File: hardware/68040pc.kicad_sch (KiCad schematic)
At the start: 1 part, among them U1 68LC040

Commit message: lock position of expansion slots
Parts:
- added J10, J11, J12, J13, J14, J15, J8, J9: EXP, 68040:EXP, symbol 68040:EXP
- added J5: DB25_Receptacle_MountingHoles, Connector_Dsub:DSUB-25_Male_Horizontal_P2.77x2.84mm_EdgePinOffset4.94mm_Housed_MountingHolesOffset7.48mm, symbol Connector:DB25_Receptacle_MountingHoles
- added J6, J7: DE9_Plug_MountingHoles, Connector_Dsub:DSUB-9_Male_Horizontal_P2.77x2.84mm_EdgePinOffset4.94mm_Housed_MountingHolesOffset7.48mm, symbol Connector:DE9_Plug_MountingHoles
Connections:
- net GND_{O}: now reaches U1.B10 (GND)
- net GND_{O}: now also U1.B13 (GND), U1.B15 (GND), U1.B17 (GND), U1.B2 (GND), U1.B4 (GND), U1.B6 (GND), U1.B8 (GND), U1.D17 (GND), U1.D2 (GND), U1.F17 (GND), U1.F2 (GND), U1.H17 (GND), U1.H2 (GND), U1.L17 (GND), U1.L2 (GND), U1.N17 (GND), U1.N2 (GND), U1.Q17 (GND), U1.Q2 (GND), U1.S15 (GND), U1.S17 (GND), U1.S2 (GND)
- net V_{CC}_{O}: now reaches U1.B14 (V_{CC})
- net V_{CC}_{O}: now also U1.B5 (V_{CC}), U1.B9 (V_{CC}), U1.C17 (V_{CC}), U1.C2 (V_{CC}), U1.G17 (V_{CC}), U1.G2 (V_{CC}), U1.M17 (V_{CC}), U1.M2 (V_{CC}), U1.R17 (V_{CC}), U1.R2 (V_{CC}), U1.S16 (V_{CC})
- net V_{CC}_{L}: now reaches U1.C10 (V_{CC})
- net V_{CC}_{L}: now also U1.C12 (V_{CC}), U1.C14 (V_{CC}), U1.C5 (V_{CC}), U1.C8 (V_{CC}), U1.H16 (V_{CC}), U1.H3 (V_{CC}), U1.J16 (V_{CC}), U1.J3 (V_{CC}), U1.L16 (V_{CC}), U1.M3 (V_{CC}), U1.R12 (V_{CC}), U1.R5 (V_{CC})
- net GND_{L}: now reaches U1.C11 (GND)
- net GND_{L}: now also U1.C13 (GND), U1.C6 (GND), U1.C7 (GND), U1.C9 (GND), U1.K16 (GND), U1.K3 (GND), U1.L3 (GND), U1.M16 (GND), U1.R11 (GND), U1.R13 (GND), U1.R4 (GND), U1.S10 (GND), U1.T4 (GND)
- net TM2: now reaches U1.K17 (TM2)
- net TM1: now reaches U1.M18 (TM1)
- net R/~{W}: now reaches U1.N16 (R/~{W})
- net TM0: now reaches U1.N18 (TM0)
- net SIZ1: now reaches U1.P16 (SIZ1)
- net SIZ0: now reaches U1.P17 (SIZ0)
- net TLN1: now reaches U1.P18 (TLN1)
- net TT1: now reaches U1.P2 (TT1)
- net TT0: now reaches U1.P3 (TT0)
- net UPA1: now reaches U1.Q1 (UPA1)
- net ~{MI}: now reaches U1.Q16 (~{MI})
- net TLN0: now reaches U1.Q18 (TLN0)
- net UPA0: now reaches U1.Q3 (UPA0)
- net ~{CIOUT}: now reaches U1.R1 (~{CIOUT})
- net GND_{P}: now reaches U1.R10 (GND)
- net GND_{P}: now also U1.R6 (GND), U1.S9 (GND)
- net PST2: now reaches U1.R14 (PST2)
- net ~{TIP}: now reaches U1.R15 (~{TIP})
- net ~{TS}: now reaches U1.R16 (~{TS})
- net ~{LOCKE}: now reaches U1.R18 (~{LOCKE})
- net ~{RSTO}: now reaches U1.R3 (~{RSTO})
- net BCLK: now reaches U1.R7 (BCLK)
- net V_{CC}_{P}: now reaches U1.R8 (V_{CC})
- net V_{CC}_{P}: now also U1.S8 (V_{CC})
- net PCLK: now reaches U1.R9 (PCLK)
- net ~{IPEND}: now reaches U1.S1 (~{IPEND})
- net ~{TBI}: now reaches U1.S11 (~{TBI})
- net SC1: now reaches U1.S12 (SC1)
- net ~{TEA}: now reaches U1.S13 (~{TEA})
- net PST1: now reaches U1.S14 (PST1)
- net ~{LOCK}: now reaches U1.S18 (~{LOCK})
- net TDI: now reaches U1.S3 (TDI)
- net TCK: now reaches U1.S4 (TCK)
- net TMS: now reaches U1.S5 (TMS)
- net ~{MDIS}: now reaches U1.S6 (~{MDIS})
- net ~{RSTI}: now reaches U1.S7 (~{RSTI})
- net ~{TCI}: now reaches U1.T10 (~{TCI})
- net ~{AVEC}: now reaches U1.T11 (~{AVEC})
- net SC0: now reaches U1.T12 (SC0)
- net ~{BG}: now reaches U1.T13 (~{BG})
- net ~{TA}: now reaches U1.T14 (~{TA})
- net PST0: now reaches U1.T15 (PST0)
- net PST3: now reaches U1.T16 (PST3)
- net ~{BB}: now reaches U1.T17 (~{BB})
- net ~{BR}: now reaches U1.T18 (~{BR})
- net TDO: now reaches U1.T2 (TDO)
- net ~{TSRT}: now reaches U1.T3 (~{TRST})
- net ~{CDIS}: now reaches U1.T5 (~{CDIS})
- net ~{IPL2}: now reaches U1.T6 (~{IPL2})
- net ~{IPL1}: now reaches U1.T7 (~{IPL1})
- net ~{IPL0}: now reaches U1.T8 (~{IPL0})
- net JS0: now reaches U1.T9 (JS0)
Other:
- moved on the sheet: U1

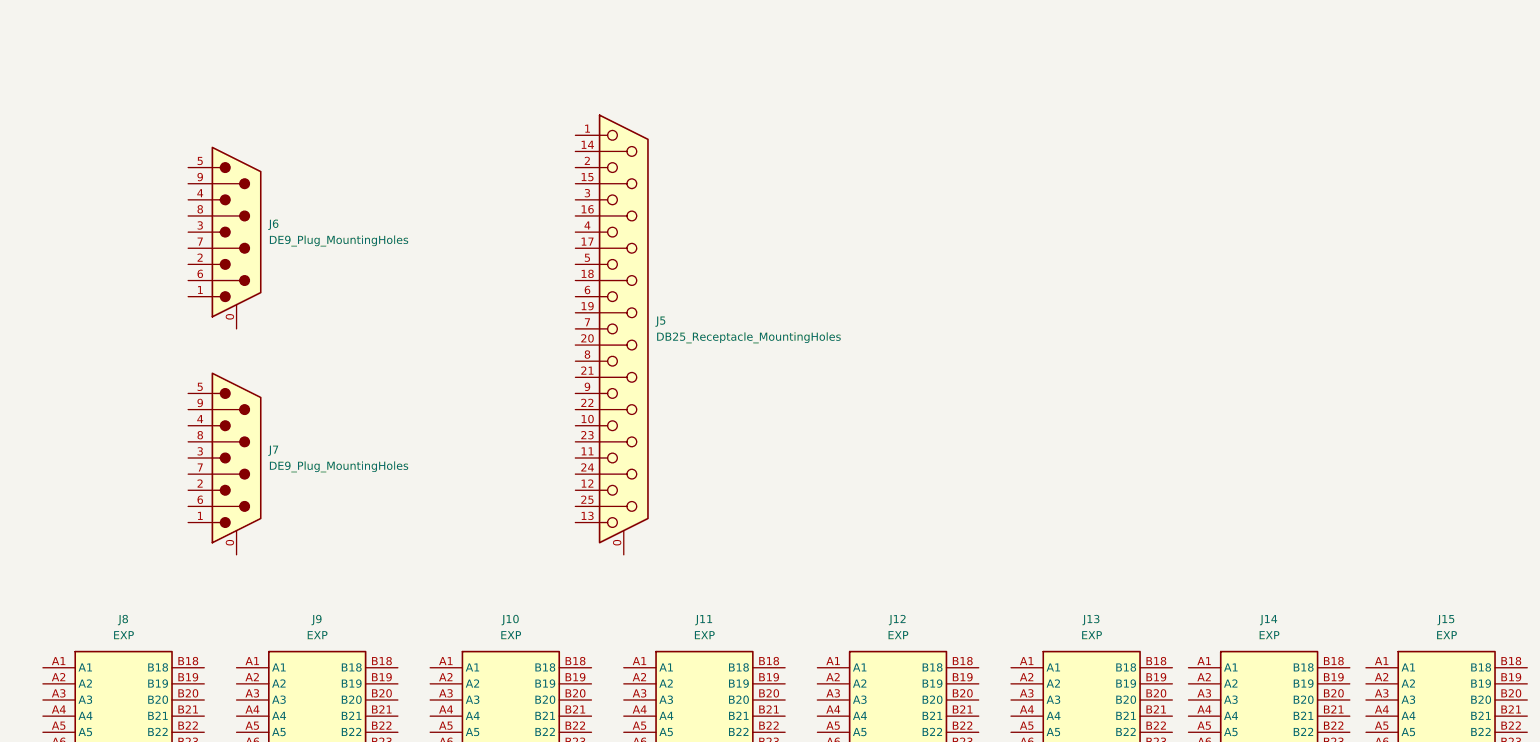
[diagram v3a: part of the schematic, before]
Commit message: fix EXP connector positioning
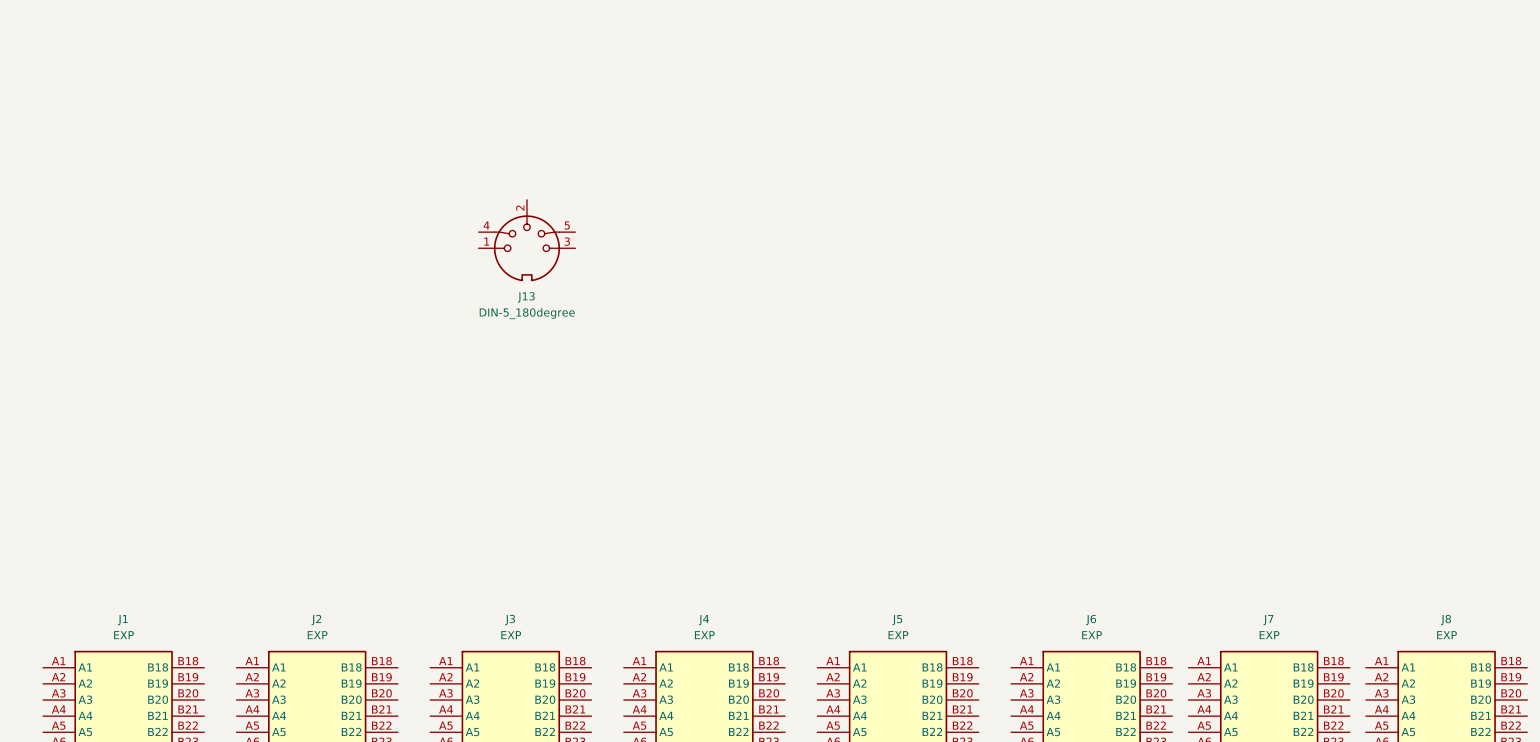
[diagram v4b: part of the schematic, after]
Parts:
- removed J5: DB25_Receptacle_MountingHoles, Connector_Dsub:DSUB-25_Male_Horizontal_P2.77x2.84mm_EdgePinOffset4.94mm_Housed_MountingHolesOffset7.48mm, symbol Connector:DB25_Receptacle_MountingHoles
- removed J6, J7: DE9_Plug_MountingHoles, Connector_Dsub:DSUB-9_Male_Horizontal_P2.77x2.84mm_EdgePinOffset4.94mm_Housed_MountingHolesOffset7.48mm, symbol Connector:DE9_Plug_MountingHoles
- added J13: DIN-5_180degree, symbol Connector:DIN-5_180degree
- renumbered J8 to J1, J9 to J2, J10 to J3, J11 to J4, J12 to J5, J13 to J6, J14 to J7, J15 to J8

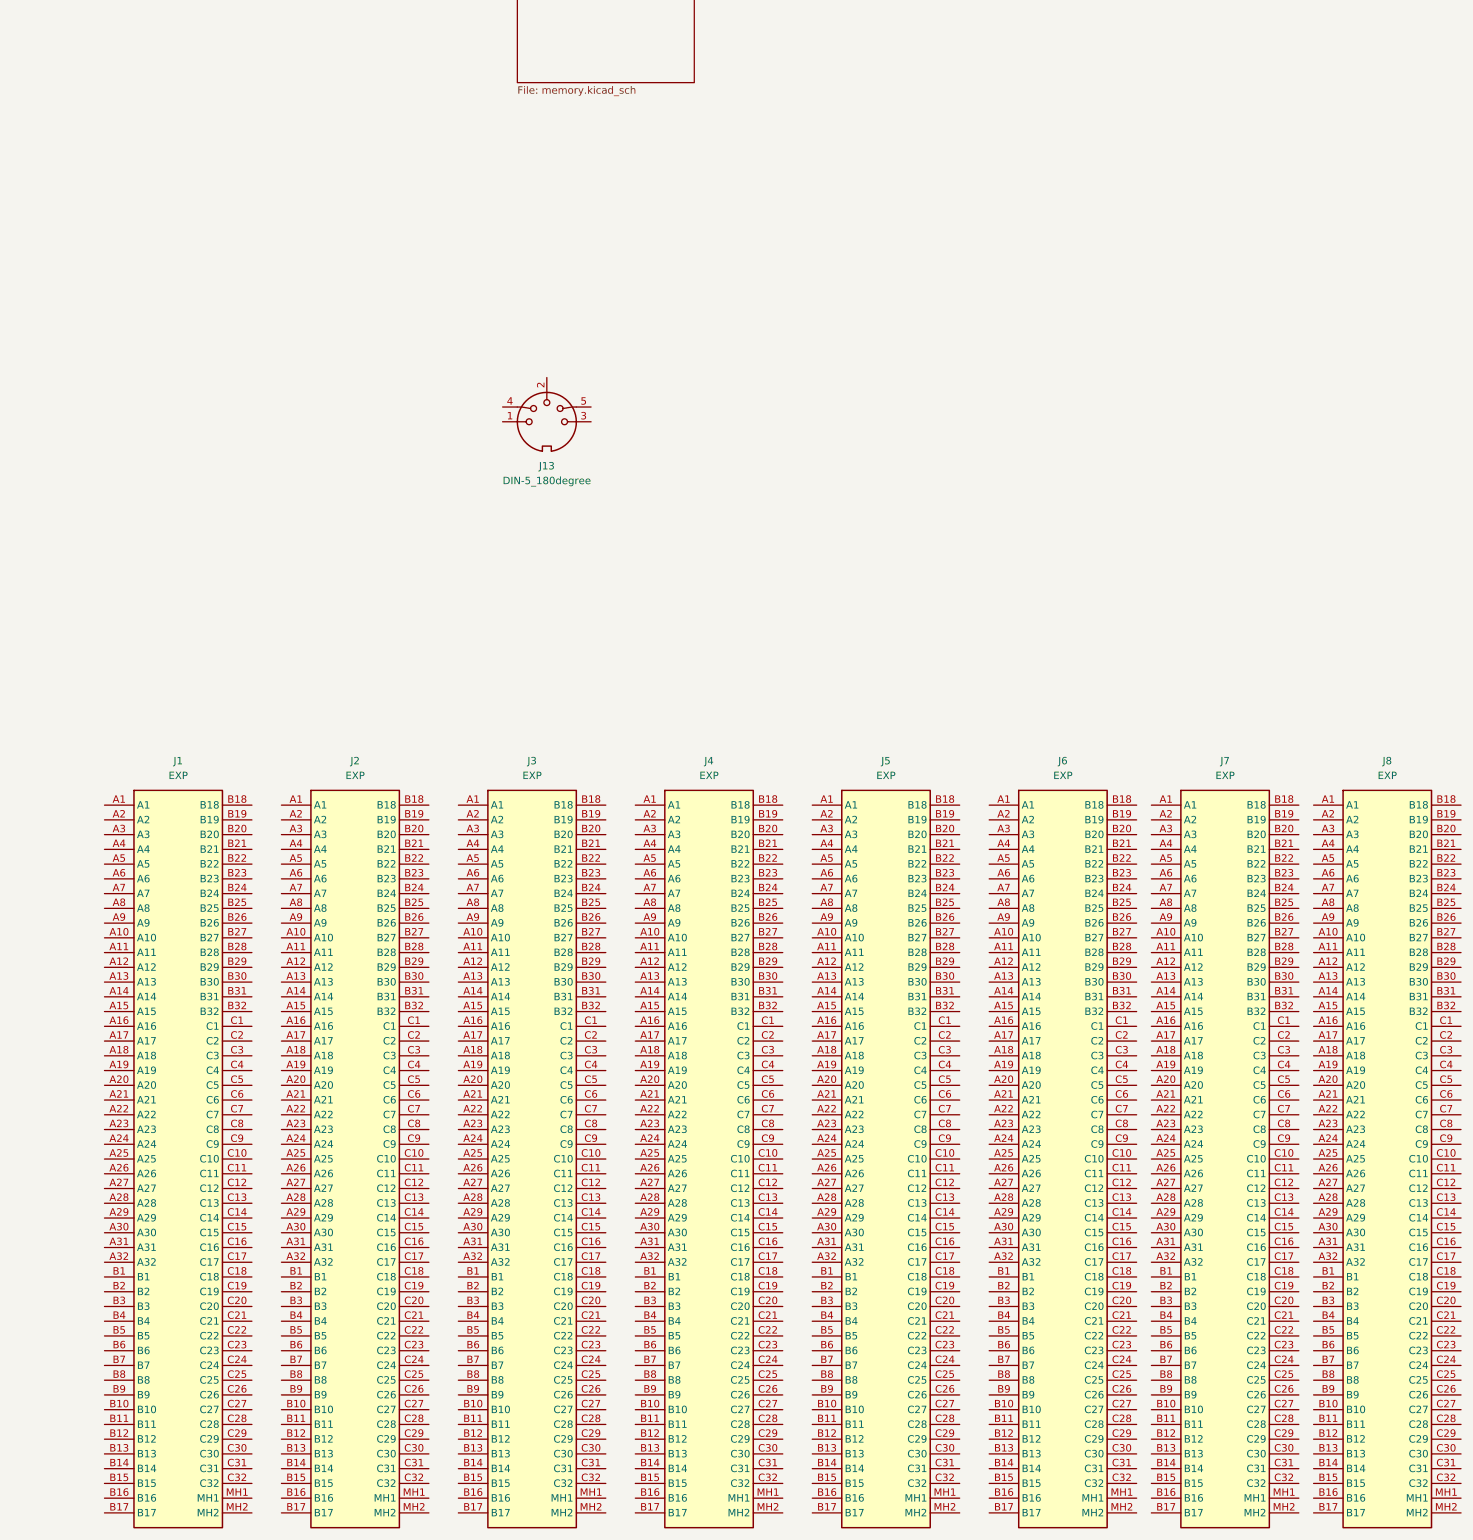
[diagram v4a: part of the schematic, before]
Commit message: Add 3d models, re-place exp slots, add components
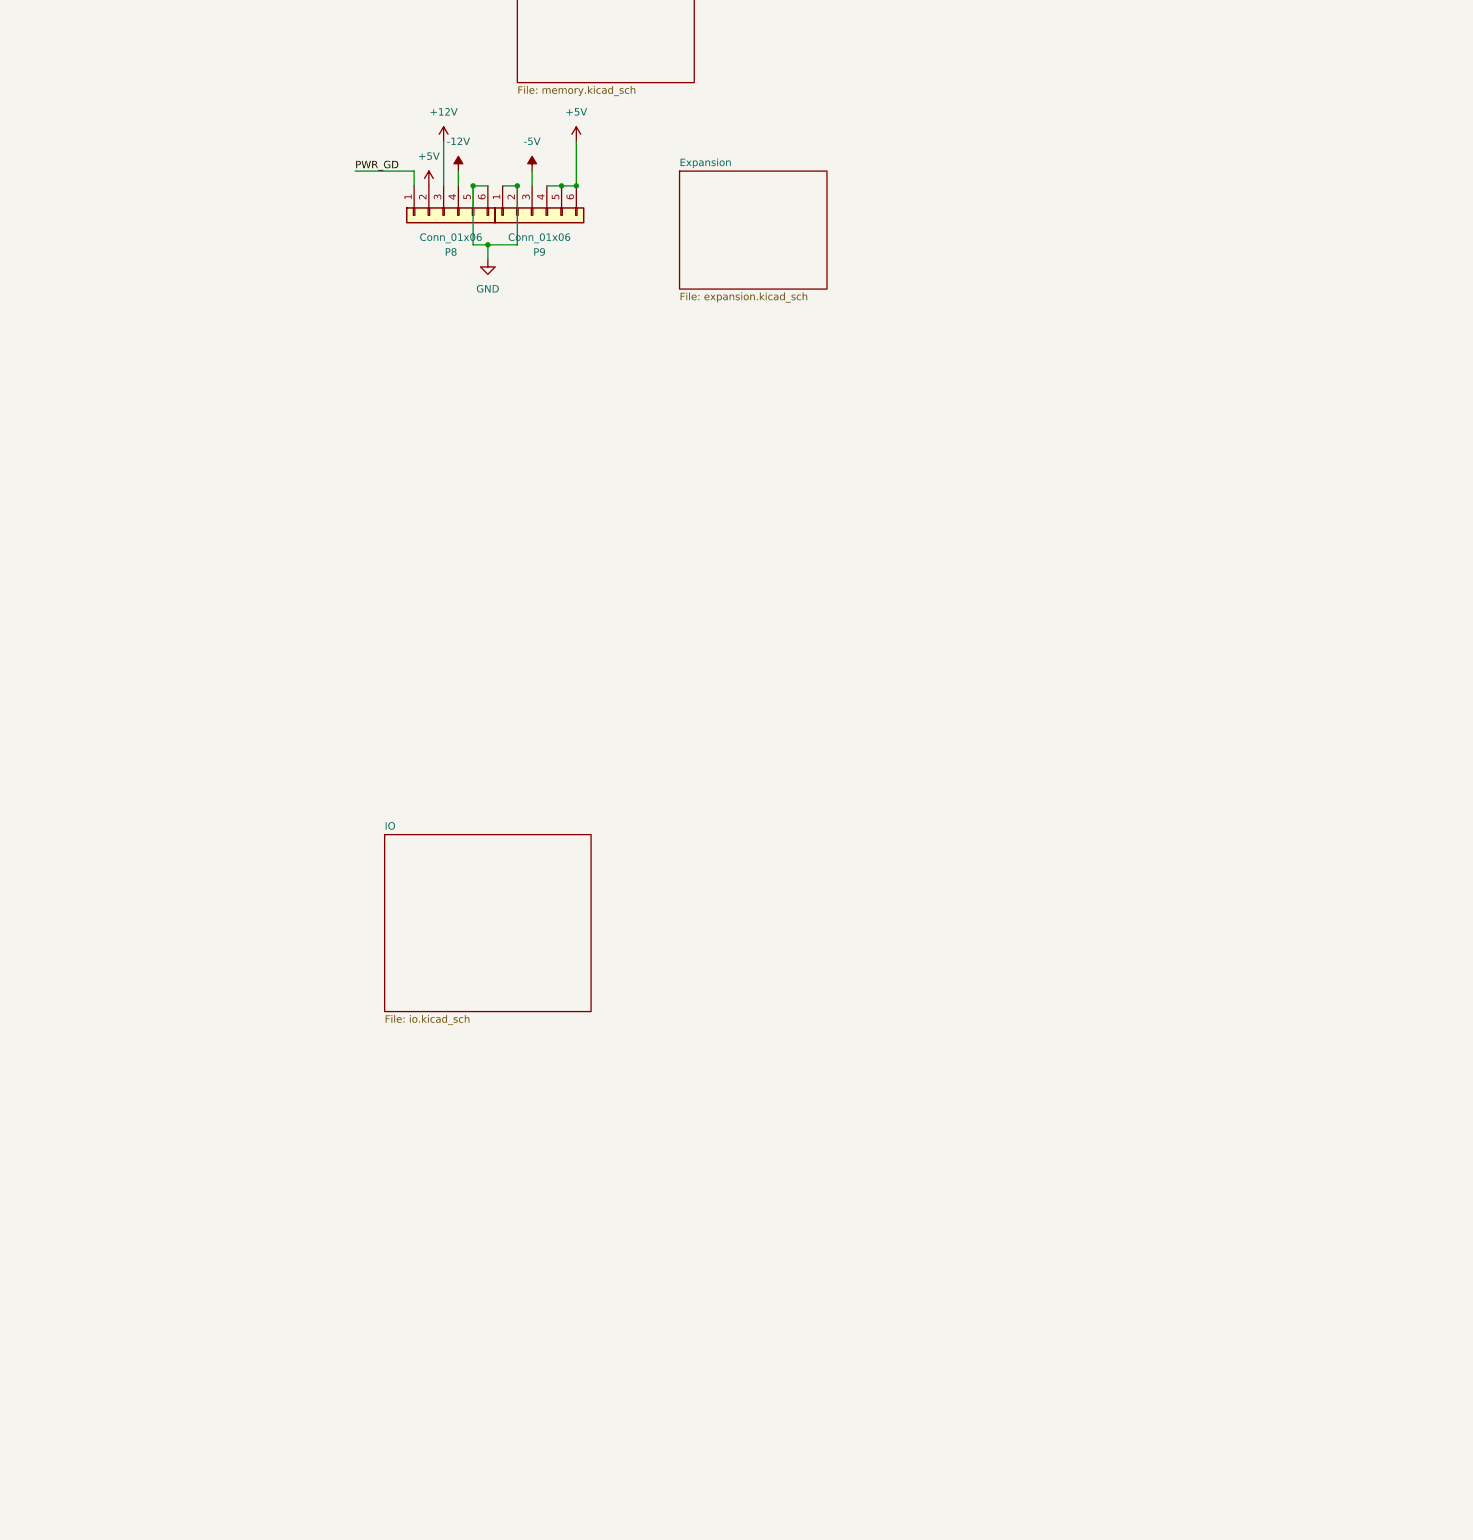
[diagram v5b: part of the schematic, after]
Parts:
- removed J1, J2, J3, J4, J5, J6, J7, J8: EXP, 68040:EXP, symbol 68040:EXP
- removed J13: DIN-5_180degree, symbol Connector:DIN-5_180degree
- added P8, P9: Conn_01x06, 68040:15-48-0106, symbol Connector_Generic:Conn_01x06
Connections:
- new net +12V: P8.3 (Pin_3)
- new net +5V: P8.2 (Pin_2), P9.4 (Pin_4), P9.5 (Pin_5), P9.6 (Pin_6)
- new net -12V: P8.4 (Pin_4)
- new net -5V: P9.3 (Pin_3)
- new net GND: P8.5 (Pin_5), P8.6 (Pin_6), P9.1 (Pin_1), P9.2 (Pin_2)
- new net PWR_GD: P8.1 (Pin_1)
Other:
- added sheet Expansion (expansion.kicad_sch)
- added sheet IO (io.kicad_sch)
